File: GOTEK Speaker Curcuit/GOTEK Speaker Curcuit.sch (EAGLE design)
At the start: 4 parts, among them T1 2N3904

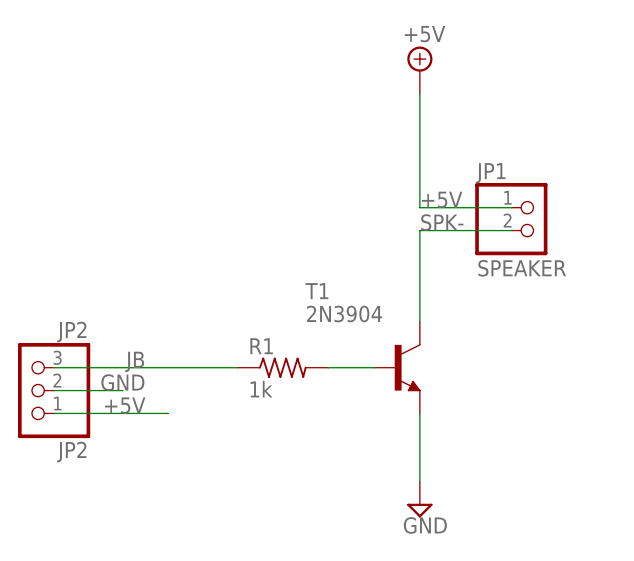
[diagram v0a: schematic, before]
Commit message: Modified GOTEK board to add 4 pin header for speaker
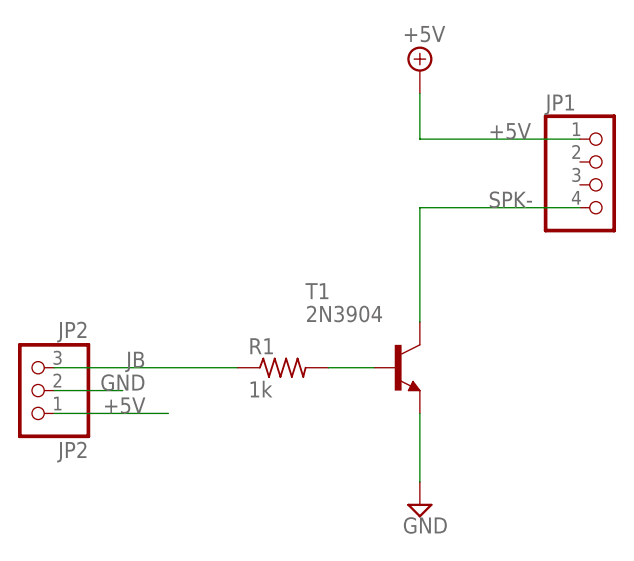
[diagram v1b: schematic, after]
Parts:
- JP1: value SPEAKER -> (none); device pinhead:PINHD-1X2 -> pinhead:PINHD-1X4
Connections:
- net SPK-: now also JP1.4; no longer JP1.2
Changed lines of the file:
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@@
 <grid distance="0.1" unitdist="inch" unit="inch" style="lines" multiple="1" display="no" altdistance="0.01" altunitdist="inch" altunit="inch"/>
 <layers>
-<layer number="1" name="Top" color="4" fill="1" visible="yes" active="no"/>
-<layer number="2" name="Route2" color="1" fill="3" visible="yes" active="no"/>
-<layer number="3" name="Route3" color="4" fill="3" visible="yes" active="no"/>
-<layer number="4" name="Route4" color="1" fill="4" visible="yes" active="no"/>
-<layer number="5" name="Route5" color="4" fill="4" visible="yes" active="no"/>
-<layer number="6" name="Route6" color="1" fill="8" visible="yes" active="no"/>
-<layer number="7" name="Route7" color="4" fill="8" visible="yes" active="no"/>
-<layer number="8" name="Route8" color="1" fill="2" visible="yes" active="no"/>
-<layer number="9" name="Route9" color="4" fill="2" visible="yes" active="no"/>
-<layer number="10" name="Route10" color="1" fill="7" visible="yes" active="no"/>
-<layer number="11" name="Route11" color="4" fill="7" visible="yes" active="no"/>
-<layer number="12" name="Route12" color="1" fill="5" visible="yes" active="no"/>
-<layer number="13" name="Route13" color="4" fill="5" visible="yes" active="no"/>
-<layer number="14" name="Route14" color="1" fill="6" visible="yes" active="no"/>
-<layer number="15" name="Route15" color="4" fill="6" visible="yes" active="no"/>
-<layer number="16" name="Bottom" color="1" fill="1" visible="yes" active="no"/>
-<layer number="17" name="Pads" color="2" fill="1" visible="yes" active="no"/>
-<layer number="18" name="Vias" color="2" fill="1" visible="yes" active="no"/>
-<layer number="19" name="Unrouted" color="6" fill="1" visible="yes" active="no"/>
-<layer number="20" name="Dimension" color="15" fill="1" visible="yes" active="no"/>
-<layer number="21" name="tPlace" color="7" fill="1" visible="yes" active="no"/>
-<layer number="22" name="bPlace" color="7" fill="1" visible="yes" active="no"/>
-<layer number="23" name="tOrigins" color="15" fill="1" visible="yes" active="no"/>
-<layer number="24" name="bOrigins" color="15" fill="1" visible="yes" active="no"/>
-<layer number="25" name="tNames" color="7" fill="1" visible="yes" active="no"/>
-<layer number="26" name="bNames" color="7" fill="1" visible="yes" active="no"/>
-<layer number="27" name="tValues" color="7" fill="1" visible="yes" active="no"/>
-<layer number="28" name="bValues" color="7" fill="1" visible="yes" active="no"/>
+<layer number="1" name="Top" color="4" fill="1" visible="no" active="no"/>
+<layer number="2" name="Route2" color="1" fill="3" visible="no" active="no"/>
+<layer number="3" name="Route3" color="4" fill="3" visible="no" active="no"/>
+<layer number="4" name="Route4" color="1" fill="4" visible="no" active="no"/>
+<layer number="5" name="Route5" color="4" fill="4" visible="no" active="no"/>
+<layer number="6" name="Route6" color="1" fill="8" visible="no" active="no"/>
+<layer number="7" name="Route7" color="4" fill="8" visible="no" active="no"/>
+<layer number="8" name="Route8" color="1" fill="2" visible="no" active="no"/>
+<layer number="9" name="Route9" color="4" fill="2" visible="no" active="no"/>
+<layer number="10" name="Route10" color="1" fill="7" visible="no" active="no"/>
+<layer number="11" name="Route11" color="4" fill="7" visible="no" active="no"/>
+<layer number="12" name="Route12" color="1" fill="5" visible="no" active="no"/>
+<layer number="13" name="Route13" color="4" fill="5" visible="no" active="no"/>
+<layer number="14" name="Route14" color="1" fill="6" visible="no" active="no"/>
+<layer number="15" name="Route15" color="4" fill="6" visible="no" active="no"/>
+<layer number="16" name="Bottom" color="1" fill="1" visible="no" active="no"/>
+<layer number="17" name="Pads" color="2" fill="1" visible="no" active="no"/>
+<layer number="18" name="Vias" color="2" fill="1" visible="no" active="no"/>
+<layer number="19" name="Unrouted" color="6" fill="1" visible="no" active="no"/>
+<layer number="20" name="Dimension" color="15" fill="1" visible="no" active="no"/>
+<layer number="21" name="tPlace" color="7" fill="1" visible="no" active="no"/>
+<layer number="22" name="bPlace" color="7" fill="1" visible="no" active="no"/>
+<layer number="23" name="tOrigins" color="15" fill="1" visible="no" active="no"/>
+<layer number="24" name="bOrigins" color="15" fill="1" visible="no" active="no"/>
+<layer number="25" name="tNames" color="7" fill="1" visible="no" active="no"/>
+<layer number="26" name="bNames" color="7" fill="1" visible="no" active="no"/>
+<layer number="27" name="tValues" color="7" fill="1" visible="no" active="no"/>
+<layer number="28" name="bValues" color="7" fill="1" visible="no" active="no"/>
 <layer number="29" name="tStop" color="7" fill="3" visible="no" active="no"/>
 <layer number="30" name="bStop" color="7" fill="6" visible="no" active="no"/>
@@
 <layer number="35" name="tGlue" color="7" fill="4" visible="no" active="no"/>
 <layer number="36" name="bGlue" color="7" fill="5" visible="no" active="no"/>
-<layer number="37" name="tTest" color="7" fill="1" visible="yes" active="no"/>
-<layer number="38" name="bTest" color="7" fill="1" visible="yes" active="no"/>
+<layer number="37" name="tTest" color="7" fill="1" visible="no" active="no"/>
+<layer number="38" name="bTest" color="7" fill="1" visible="no" active="no"/>
 <layer number="39" name="tKeepout" color="4" fill="11" visible="no" active="no"/>
 <layer number="40" name="bKeepout" color="1" fill="11" visible="no" active="no"/>
@@
 <layer number="44" name="Drills" color="7" fill="1" visible="no" active="no"/>
 <layer number="45" name="Holes" color="7" fill="1" visible="no" active="no"/>
-<layer number="46" name="Milling" color="3" fill="1" visible="yes" active="no"/>
-<layer number="47" name="Measures" color="7" fill="1" visible="yes" active="no"/>
-<layer number="48" name="Document" color="7" fill="1" visible="yes" active="no"/>
-<layer number="49" name="Reference" color="7" fill="1" visible="yes" active="no"/>
-<layer number="51" name="tDocu" color="7" fill="1" visible="yes" active="no"/>
-<layer number="52" name="bDocu" color="7" fill="1" visible="yes" active="no"/>
+<layer number="46" name="Milling" color="3" fill="1" visible="no" active="no"/>
+<layer number="47" name="Measures" color="7" fill="1" visible="no" active="no"/>
+<layer number="48" name="Document" color="7" fill="1" visible="no" active="no"/>
+<layer number="49" name="Reference" color="7" fill="1" visible="no" active="no"/>
+<layer number="51" name="tDocu" color="7" fill="1" visible="no" active="no"/>
+<layer number="52" name="bDocu" color="7" fill="1" visible="no" active="no"/>
 <layer number="88" name="SimResults" color="9" fill="1" visible="yes" active="yes"/>
 <layer number="89" name="SimProbes" color="9" fill="1" visible="yes" active="yes"/>
@@
 </classes>
 <parts>
-<part name="JP1" library="pinhead" library_urn="urn:adsk.eagle:library:325" deviceset="PINHD-1X2" device="" package3d_urn="urn:adsk.eagle:package:22435/2" value="SPEAKER"/>
 <part name="JP2" library="pinhead" library_urn="urn:adsk.eagle:library:325" deviceset="PINHD-1X3" device="" package3d_urn="urn:adsk.eagle:package:22458/2" value="JP2"/>
 <part name="T1" library="transistor" library_urn="urn:adsk.eagle:library:402" deviceset="2N3904" device="" package3d_urn="urn:adsk.eagle:package:28523/2"/>
@@
 <part name="SUPPLY1" library="supply2" library_urn="urn:adsk.eagle:library:372" deviceset="GND" device=""/>
 <part name="SUPPLY2" library="supply2" library_urn="urn:adsk.eagle:library:372" deviceset="+5V" device=""/>
+<part name="JP1" library="pinhead" library_urn="urn:adsk.eagle:library:325" deviceset="PINHD-1X4" device="" package3d_urn="urn:adsk.eagle:package:22407/2"/>
 </parts>
 <sheets>
@@
 </plain>
 <instances>
-<instance part="JP1" gate="G$1" x="73.66" y="68.58" smashed="yes">
-<attribute name="NAME" x="67.31" y="74.295" size="1.778" layer="95"/>
-<attribute name="VALUE" x="67.31" y="63.5" size="1.778" layer="96"/>
-</instance>
 <instance part="JP2" gate="A" x="17.78" y="50.8" smashed="yes" rot="R180">
 <attribute name="NAME" x="24.13" y="45.085" size="1.778" layer="95" rot="R180"/>
@@
 <attribute name="VALUE" x="59.055" y="89.535" size="1.778" layer="96"/>
 </instance>
+<instance part="JP1" gate="A" x="81.28" y="73.66" smashed="yes">
+<attribute name="NAME" x="74.93" y="81.915" size="1.778" layer="95"/>
+<attribute name="VALUE" x="74.93" y="66.04" size="1.778" layer="96"/>
+</instance>
 </instances>
 <busses>
@@
 </segment>
 <segment>
-<pinref part="JP1" gate="G$1" pin="1"/>
-<wire x1="71.12" y1="71.12" x2="60.96" y2="71.12" width="0.1524" layer="91"/>
-<label x="60.96" y="71.12" size="1.778" layer="95"/>
+<pinref part="JP1" gate="A" pin="1"/>
+<wire x1="78.74" y1="78.74" x2="60.96" y2="78.74" width="0.1524" layer="91"/>
+<label x="68.58" y="78.74" size="1.778" layer="95"/>
 <pinref part="SUPPLY2" gate="+5V" pin="+5V"/>
-<wire x1="60.96" y1="71.12" x2="60.96" y2="83.82" width="0.1524" layer="91"/>
+<wire x1="60.96" y1="78.74" x2="60.96" y2="83.82" width="0.1524" layer="91"/>
 </segment>
 </net>
@@
 <net name="SPK-" class="0">
 <segment>
-<pinref part="JP1" gate="G$1" pin="2"/>
-<wire x1="60.96" y1="68.58" x2="71.12" y2="68.58" width="0.1524" layer="91"/>
-<label x="60.96" y="68.58" size="1.778" layer="95"/>
+<pinref part="JP1" gate="A" pin="4"/>
+<wire x1="78.74" y1="71.12" x2="60.96" y2="71.12" width="0.1524" layer="91"/>
+<label x="68.58" y="71.12" size="1.778" layer="95"/>
 <pinref part="T1" gate="G1" pin="C"/>
-<wire x1="60.96" y1="58.42" x2="60.96" y2="68.58" width="0.1524" layer="91"/>
+<wire x1="60.96" y1="58.42" x2="60.96" y2="71.12" width="0.1524" layer="91"/>
 </segment>
 </net>
